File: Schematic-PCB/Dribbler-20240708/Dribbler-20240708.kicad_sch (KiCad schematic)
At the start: 8 parts, among them J1 Conn_01x04_Pin, J2 Conn_01x02_Pin, J3 Conn_01x02_Pin

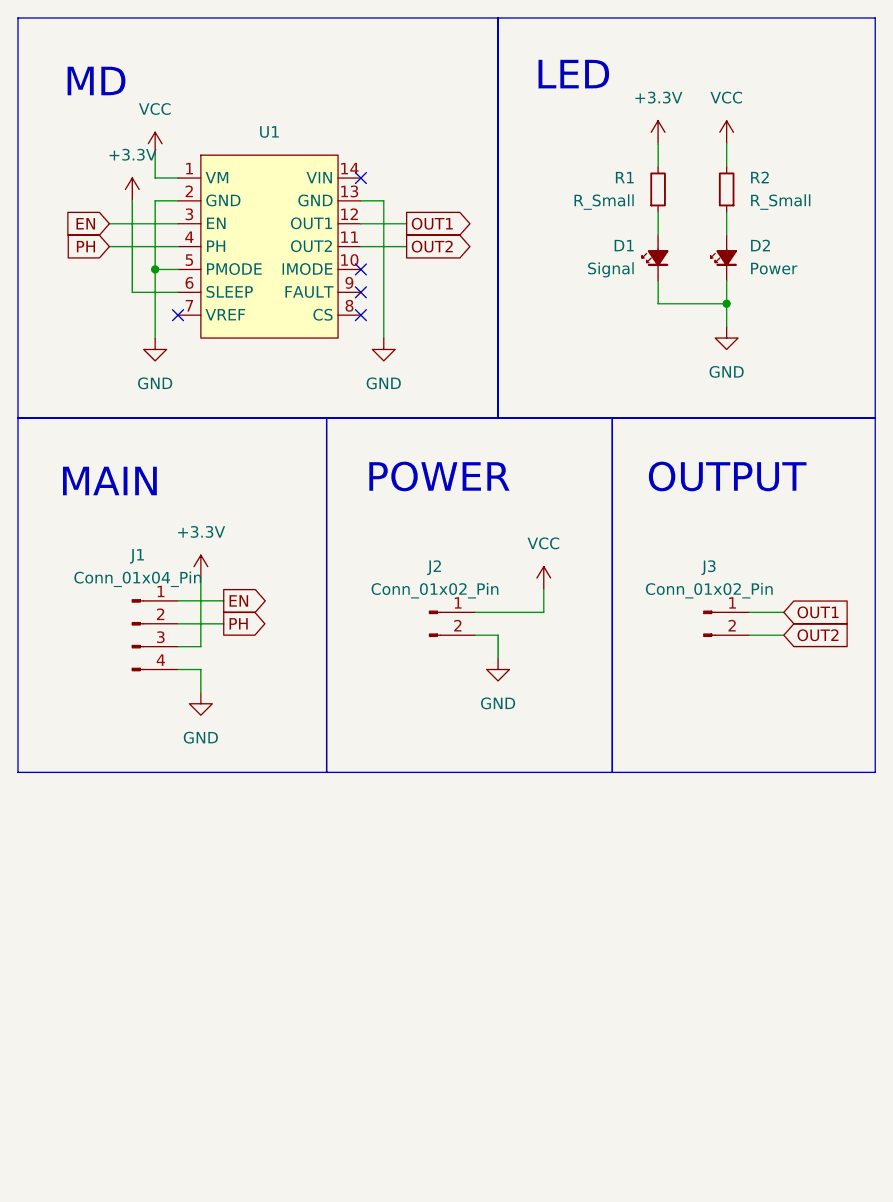
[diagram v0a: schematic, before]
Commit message: ドリブラの回路図を修正した
ENの1ピン制御に切り替えた
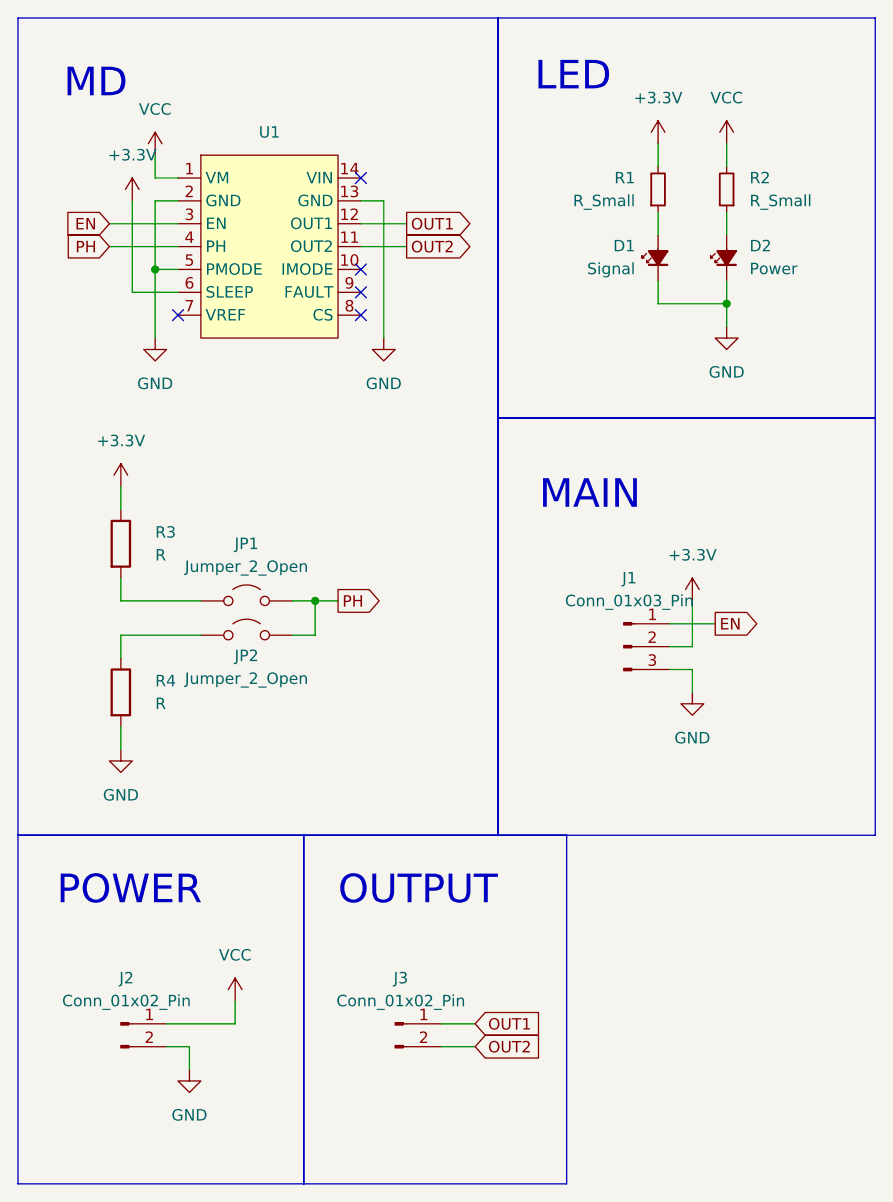
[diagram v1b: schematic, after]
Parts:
- removed J1: Conn_01x04_Pin, symbol Connector:Conn_01x04_Pin
- added J1: Conn_01x03_Pin, symbol Connector:Conn_01x03_Pin
- added JP1, JP2: Jumper_2_Open, symbol Jumper:Jumper_2_Open
- added R3, R4: R, symbol Device:R
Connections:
- net +3.3V: now also J1.2 (Pin_2), R3.1
- net EN: now also J1.1 (Pin_1)
- net GND: now also J1.3 (Pin_3), R4.2
- net PH: now also JP1.2 (B), JP2.2 (B)
- new net: JP2.1 (A), R4.1
- new net: JP1.1 (A), R3.2
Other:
- moved on the sheet: J2, J3

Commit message: 回路と設計を進めた
3DモデルのファイルとかドリブラーのPCBデザインとか
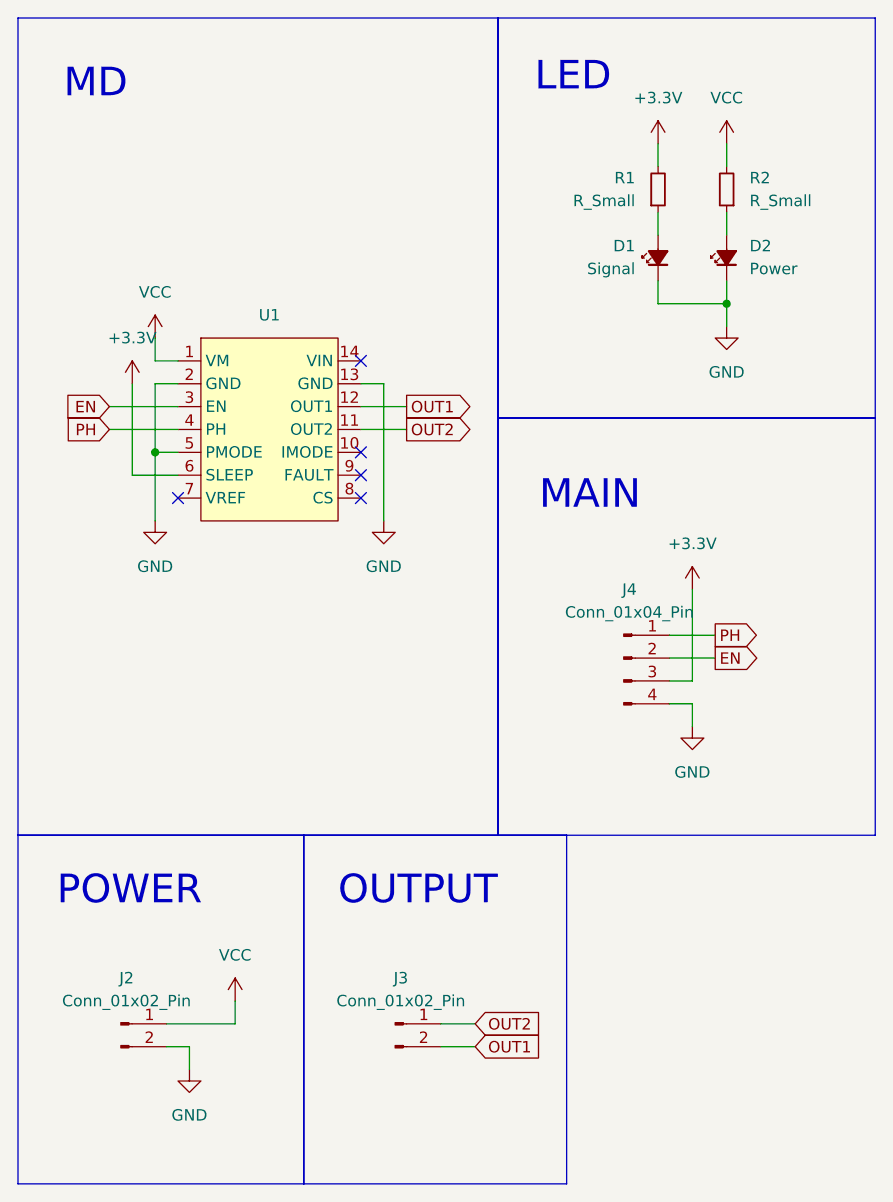
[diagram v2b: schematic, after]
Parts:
- removed J1: Conn_01x03_Pin, symbol Connector:Conn_01x03_Pin
- removed JP1, JP2: Jumper_2_Open, symbol Jumper:Jumper_2_Open
- removed R3, R4: R, symbol Device:R
- added J4: Conn_01x04_Pin, Connector_JST:JST_XH_B4B-XH-A_1x04_P2.50mm_Vertical, symbol Connector:Conn_01x04_Pin
- D1, D2: footprint (none) -> LED_SMD:LED_0805_2012Metric
- J2, J3: footprint (none) -> Connector_JST:JST_XH_B2B-XH-A_1x02_P2.50mm_Vertical
- R1, R2: footprint (none) -> Resistor_THT:R_Axial_DIN0207_L6.3mm_D2.5mm_P7.62mm_Horizontal
- U1: footprint (none) -> @2024-Dribbler:DRV8874 module
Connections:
- net +3.3V: now also J4.3 (Pin_3)
- net EN: now also J4.2 (Pin_2)
- net GND: now also J4.4 (Pin_4)
- net OUT1: now also J3.2 (Pin_2); no longer J3.1 (Pin_1)
- net OUT2: now also J3.1 (Pin_1); no longer J3.2 (Pin_2)
- net PH: now also J4.1 (Pin_1)
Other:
- moved on the sheet: U1

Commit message: ドリブラー基板の外形とかを仮完成させた
めちゃミニミニ基板になったよ
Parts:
- J2, J3: footprint Connector_JST:JST_XH_B2B-XH-A_1x02_P2.50mm_Vertical -> Connector_JST:JST_XH_S2B-XH-A-1_1x02_P2.50mm_Horizontal
- R1, R2: footprint Resistor_THT:R_Axial_DIN0207_L6.3mm_D2.5mm_P7.62mm_Horizontal -> Resistor_SMD:R_0603_1608Metric
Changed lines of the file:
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@@
 			)
 		)
-		(property "Footprint" "Resistor_THT:R_Axial_DIN0207_L6.3mm_D2.5mm_P7.62mm_Horizontal"
+		(property "Footprint" "Resistor_SMD:R_0603_1608Metric"
 			(at 83.82 31.75 0)
 			(effects
@@
 			)
 		)
-		(property "Footprint" "Resistor_THT:R_Axial_DIN0207_L6.3mm_D2.5mm_P7.62mm_Horizontal"
+		(property "Footprint" "Resistor_SMD:R_0603_1608Metric"
 			(at 91.44 31.75 0)
 			(effects
@@
 			)
 		)
-		(property "Footprint" "Connector_JST:JST_XH_B2B-XH-A_1x02_P2.50mm_Vertical"
+		(property "Footprint" "Connector_JST:JST_XH_S2B-XH-A-1_1x02_P2.50mm_Horizontal"
 			(at 24.13 124.46 0)
 			(effects
@@
 			)
 		)
-		(property "Footprint" "Connector_JST:JST_XH_B2B-XH-A_1x02_P2.50mm_Vertical"
+		(property "Footprint" "Connector_JST:JST_XH_S2B-XH-A-1_1x02_P2.50mm_Horizontal"
 			(at 54.61 124.46 0)
 			(effects
@@
 		)
 		(instances
-			(project ""
+			(project "Dribbler-20240708"
 				(path "/0a3116e9-faad-4936-b617-c6a76f14ef35"
 					(reference "J4")

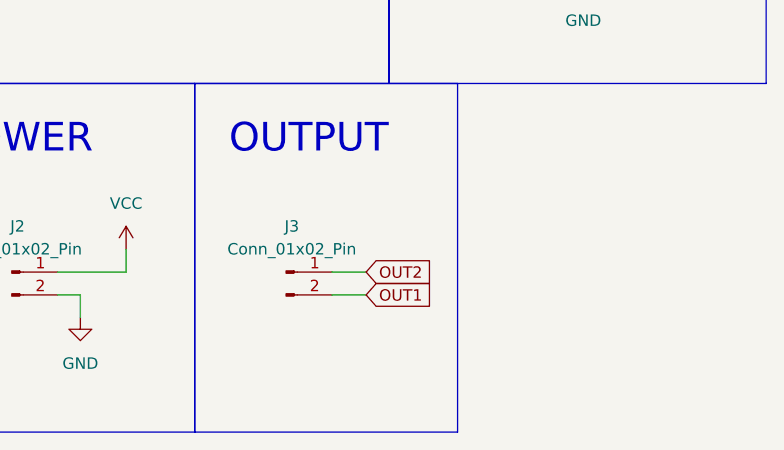
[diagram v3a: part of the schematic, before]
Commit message: ドリブラー基板のPCBを完成させた
設計通りの基板外形でやったよ
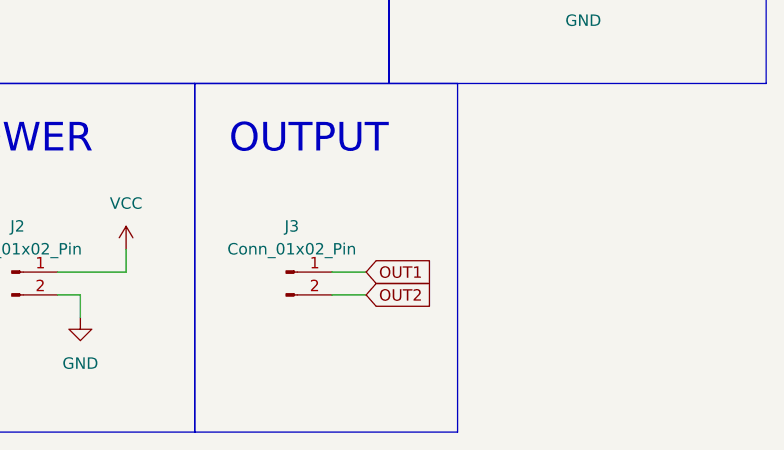
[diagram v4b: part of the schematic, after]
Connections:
- net OUT1: now also J3.1 (Pin_1); no longer J3.2 (Pin_2)
- net OUT2: now also J3.2 (Pin_2); no longer J3.1 (Pin_1)
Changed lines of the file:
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@@
 	(global_label "OUT2"
 		(shape input)
-		(at 63.5 124.46 0)
+		(at 63.5 127 0)
 		(fields_autoplaced yes)
 		(effects
@@
 		)
 		(property "Intersheetrefs" "${INTERSHEET_REFS}"
-			(at 71.691 124.46 0)
+			(at 71.691 127 0)
 			(effects
 				(font
@@
 	(global_label "OUT1"
 		(shape input)
-		(at 63.5 127 0)
+		(at 63.5 124.46 0)
 		(fields_autoplaced yes)
 		(effects
@@
 		)
 		(property "Intersheetrefs" "${INTERSHEET_REFS}"
-			(at 71.691 127 0)
+			(at 71.691 124.46 0)
 			(effects
 				(font

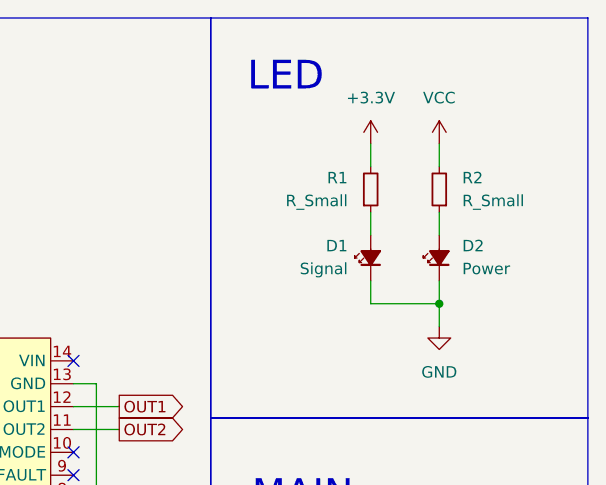
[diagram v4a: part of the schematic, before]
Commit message: ドリブラー基板の発注用ファイルを作成した
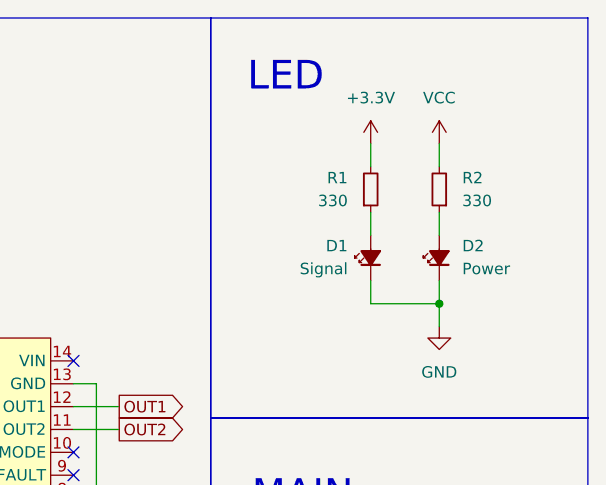
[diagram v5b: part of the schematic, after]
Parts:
- R1, R2: value R_Small -> 330
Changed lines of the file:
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@@
 			)
 		)
-		(property "Value" "R_Small"
+		(property "Value" "330"
 			(at 81.28 33.02 0)
 			(effects
@@
 			)
 		)
-		(property "Value" "R_Small"
+		(property "Value" "330"
 			(at 93.98 33.02 0)
 			(effects

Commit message: clean: コンフリクトを修正
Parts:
- D1, D2: footprint LED_SMD:LED_0805_2012Metric -> LED_SMD:LED_0603_1608Metric
- J1: renamed from J2; value Conn_01x02_Pin -> Conn_PWR
- J2: renamed from J3; value Conn_01x02_Pin -> Conn_OUT
- J3: renamed from J4; value Conn_01x04_Pin -> Conn_Main
- U1: footprint @2024-Dribbler:DRV8874 module -> @2024TOINIOT2-Dribbler:DRV8874 module
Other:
- note removed: "LED"
- note removed: "MAIN"
- note removed: "MD"
- note removed: "OUTPUT"
- note removed: "POWER"
- moved on the sheet: J1, J2
